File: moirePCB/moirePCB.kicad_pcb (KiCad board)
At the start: 2 copper layers, 37.1 x 85.7 mm, 25 parts, among them J1 USB_C_Receptacle, SW1 SW_Push_SPDT, SW3 SW_DPDT_x2, U1 ESP32-PICO-D4, U2 BQ24075RGT, U3 UA78M33, U4 RFM95W-915S2, U5 CH340E, Y2 32.768kHz

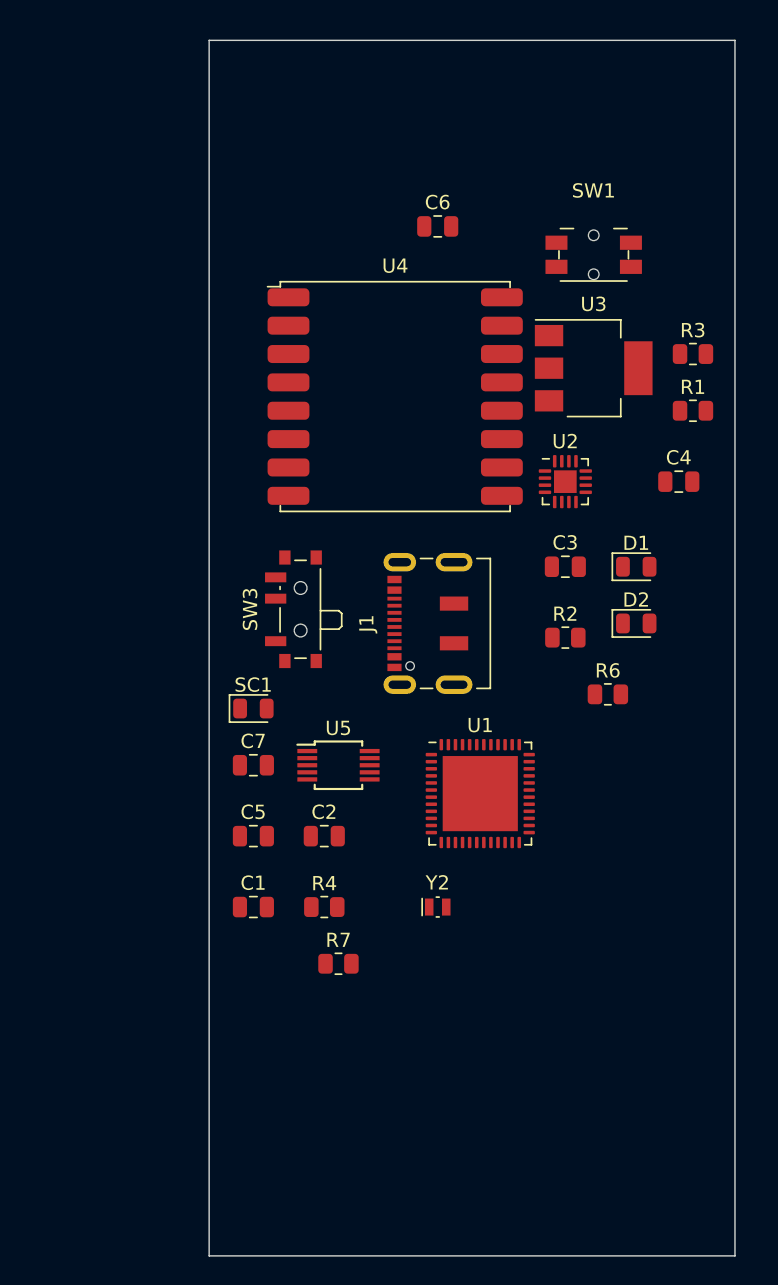
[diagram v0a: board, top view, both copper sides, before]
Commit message: new placement and battery footprint
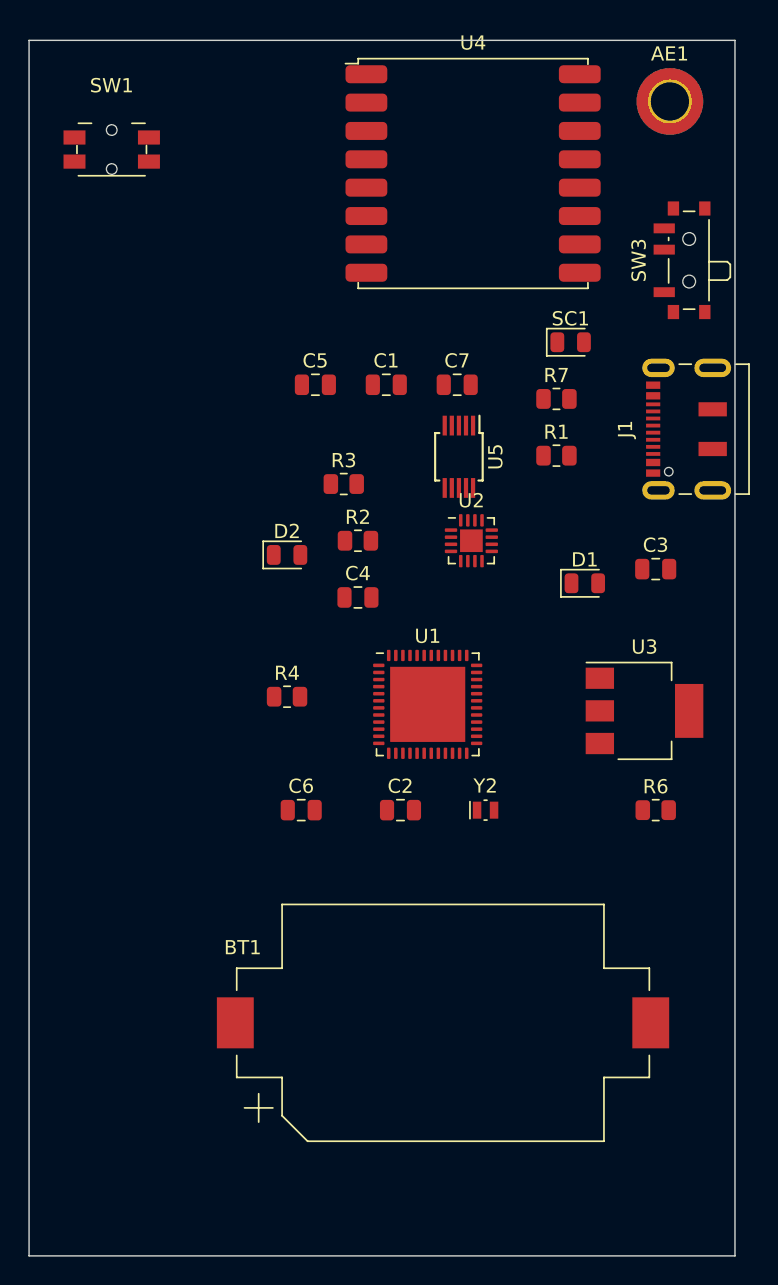
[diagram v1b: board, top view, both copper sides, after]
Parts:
- added AE1: T1-915M Antenna, MountingHole:MountingHole_2.7mm_M2.5_DIN965_Pad_TopBottom, F.Cu at (85.0, 33.0)
- added BT1: Battery_Cell, Battery:BatteryHolder_Keystone_1060_1x2032, F.Cu at (69.0, 98.0)
- moved R7 42.7 mm to (77.0, 54.0)
- moved C6 42.3 mm to (59.0, 83.0)
- moved C1 38.0 mm to (65.0, 53.0)
- moved SW3 36.8 mm to (86.0, 44.2)
- moved SW1 34.8 mm to (45.6, 36.4)
- moved SC1 34.2 mm to (78.0, 50.0)
- moved C5 32.1 mm to (60.0, 53.0)
- moved C7 30.4 mm to (70.0, 53.0)
- moved R3 26.3 mm to (62.0, 60.0)
- moved D2 25.1 mm to (58.0, 65.0)
- moved U3 24.4 mm to (83.2, 76.0)
- moved C4 24.1 mm to (63.0, 68.0)
- moved U5 23.4 mm to (70.1, 58.1), turned to -90 degrees
- moved J1 22.8 mm to (86.9, 56.1)
- moved U4 16.7 mm to (71.1, 38.1)
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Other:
- board size 37.1 x 85.7 mm -> 49.8 x 85.7 mm

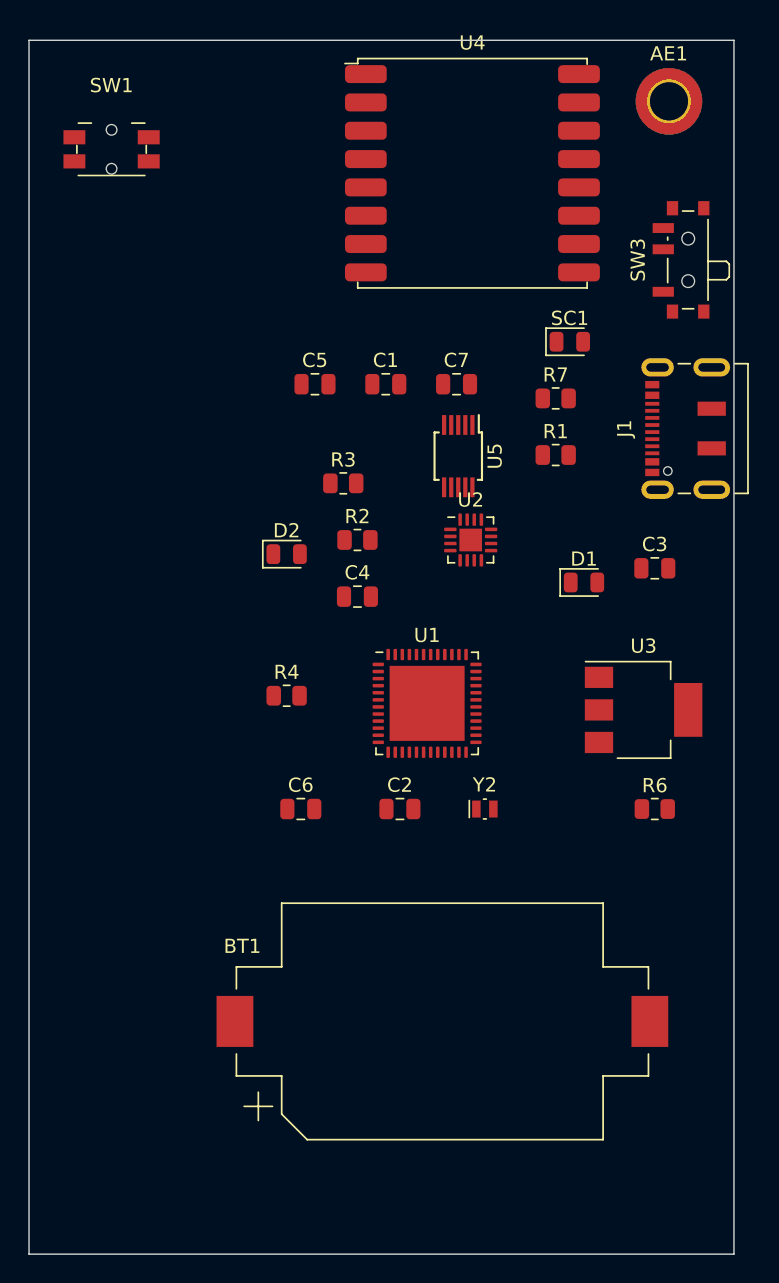
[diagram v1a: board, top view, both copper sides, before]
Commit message: ground plane, routing, comp layout
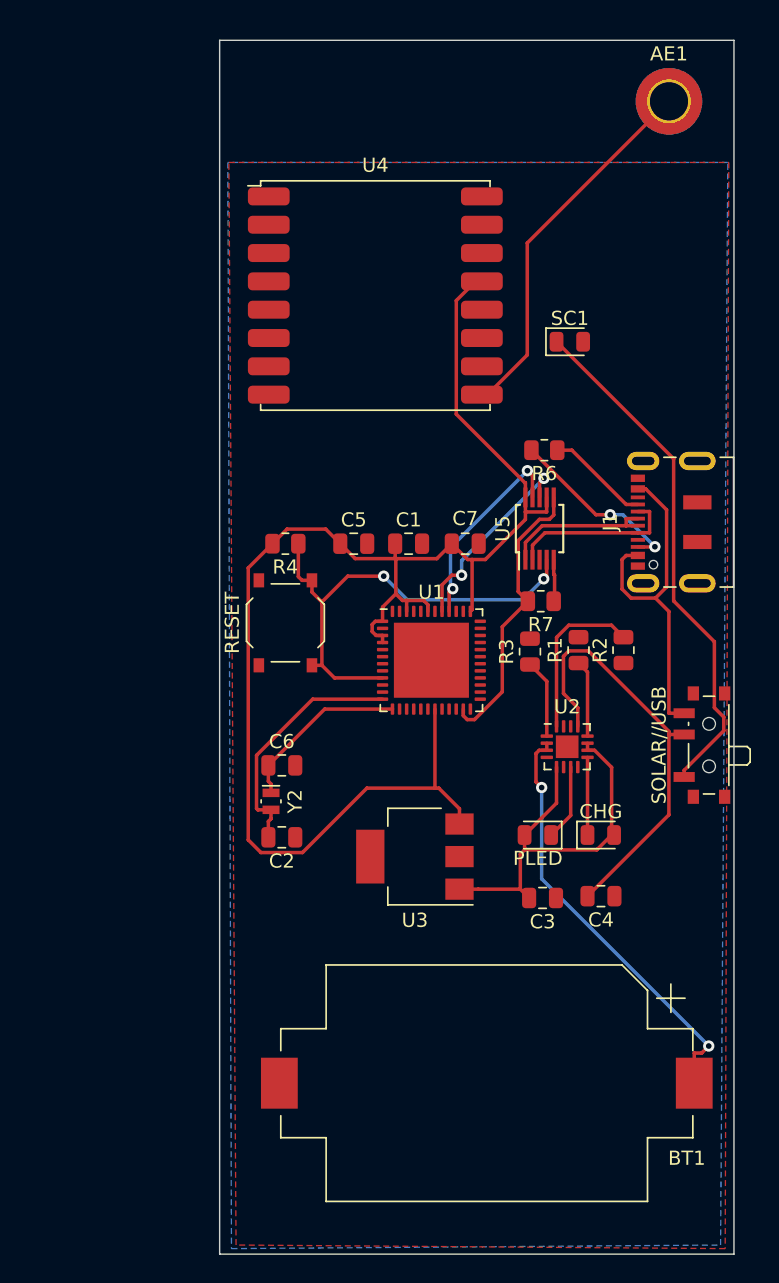
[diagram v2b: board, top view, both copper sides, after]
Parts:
- removed SW1: SW_Push_SPDT, Button_Switch_SMD:Panasonic_EVQPUL_EVQPUC
- added RESET: SW_Push, Button_Switch_SMD:SW_Push_1P1T_XKB_TS-1187A, F.Cu at (57.9, 69.8)
- moved SOLAR//USB 34.3 mm to (87.5, 78.5)
- moved CHG 29.8 mm to (80.2, 84.8)
- moved C4 27.3 mm to (80.2, 89.2), turned to 180 degrees
- moved R6 26.5 mm to (76.2, 57.7), turned to 180 degrees
- moved C3 24.6 mm to (76.1, 89.3), turned to 180 degrees
- moved R2 20.3 mm to (81.8, 71.8), turned to 90 degrees
- moved U3 19.2 mm to (67.1, 86.4), turned to 180 degrees
- moved PLED 18.1 mm to (75.7, 84.8), turned to 180 degrees
- moved R3 17.7 mm to (75.2, 71.9), turned to 90 degrees
- moved U2 16.1 mm to (77.8, 78.6)
- moved Y2 15.1 mm to (56.9, 82.5), turned to -90 degrees
- moved R7 14.4 mm to (75.9, 68.3), turned to 180 degrees
- moved R1 13.9 mm to (78.6, 71.8), turned to 90 degrees
- moved C5 11.6 mm to (62.7, 64.3)
- moved C1 11.4 mm to (66.6, 64.3)
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- renumbered D2 to CHG, D1 to PLED, SW3 to SOLAR//USB
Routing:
- net VCC: track 0.00 -> 105.7 mm
- net Net-(SC1-+): track 0.00 -> 36.8 mm
- net /EN: track 0.00 -> 34.2 mm, vias 0 -> 2
- net Net-(BT1-+): track 0.00 -> 30.4 mm, vias 0 -> 2
- net Net-(SW3A-B): track 0.00 -> 30.4 mm
- net Net-(D1-A): track 0.00 -> 29.1 mm
- net Net-(AE1-A): track 0.00 -> 26.4 mm
- net /USB5V: track 0.00 -> 24.7 mm
- net /IO0: track 0.00 -> 20.4 mm
- net Net-(U1-IO32): track 0.00 -> 17.4 mm
- net /RX: track 0.00 -> 14.4 mm, vias 0 -> 2
- net /TX: track 0.00 -> 14.3 mm, vias 0 -> 2
- net Net-(J1-CC1): track 0.00 -> 12.8 mm, vias 0 -> 2
- net Net-(U1-IO33): track 0.00 -> 12.4 mm
- net /D-: track 0.00 -> 12.0 mm
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- added copper zone on B.Cu, net GND
- added copper zone on F.Cu, net GND
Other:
- board size 49.8 x 85.7 mm -> 36.3 x 85.7 mm

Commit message: vias for esp32
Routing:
- net GND: track 0.00 -> 0.22 mm, vias 0 -> 9
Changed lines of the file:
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@@
   (segment (start 70.3566 66.4895) (end 70.3566 65.462) (width 0.25) (layer "B.Cu") (net 37))
   (segment (start 70.3566 65.462) (end 76.171 59.6476) (width 0.25) (layer "B.Cu") (net 37))
+  (segment (start 68.224 72.492) (end 68.216 72.5) (width 0.25) (layer "F.Cu") (net 43))
+  (segment (start 68.2 72.5) (end 68.2 72.516) (width 0.25) (layer "F.Cu") (net 43))
+  (segment (start 68.2 72.516) (end 68.326 72.39) (width 0.25) (layer "F.Cu") (net 43))
+  (segment (start 68.216 72.5) (end 68.2 72.5) (width 0.25) (layer "F.Cu") (net 43))
+  (via (at 69.6 71.2) (size 0.8) (drill 0.4) (layers "F.Cu" "B.Cu") (net 43))
+  (via (at 66.9 71.2) (size 0.8) (drill 0.4) (layers "F.Cu" "B.Cu") (net 43))
+  (via (at 66.9 72.5) (size 0.8) (drill 0.4) (layers "F.Cu" "B.Cu") (net 43))
+  (via (at 68.2 72.5) (size 0.8) (drill 0.4) (layers "F.Cu" "B.Cu") (net 43))
+  (via (at 68.2 71.2) (size 0.8) (drill 0.4) (layers "F.Cu" "B.Cu") (net 43))
+  (via (at 69.6 72.5) (size 0.8) (drill 0.4) (layers "F.Cu" "B.Cu") (net 43))
+  (via (at 69.6 73.8) (size 0.8) (drill 0.4) (layers "F.Cu" "B.Cu") (net 43))
+  (via (at 66.9 73.8) (size 0.8) (drill 0.4) (layers "F.Cu" "B.Cu") (net 43))
+  (via (at 68.2 73.8) (size 0.8) (drill 0.4) (layers "F.Cu" "B.Cu") (net 43))
   (segment (start 76.373 73.9835) (end 76.373 77.851) (width 0.25) (layer "F.Cu") (net 44))
   (segment (start 75.184 72.7945) (end 76.373 73.9835) (width 0.25) (layer "F.Cu") (net 44))

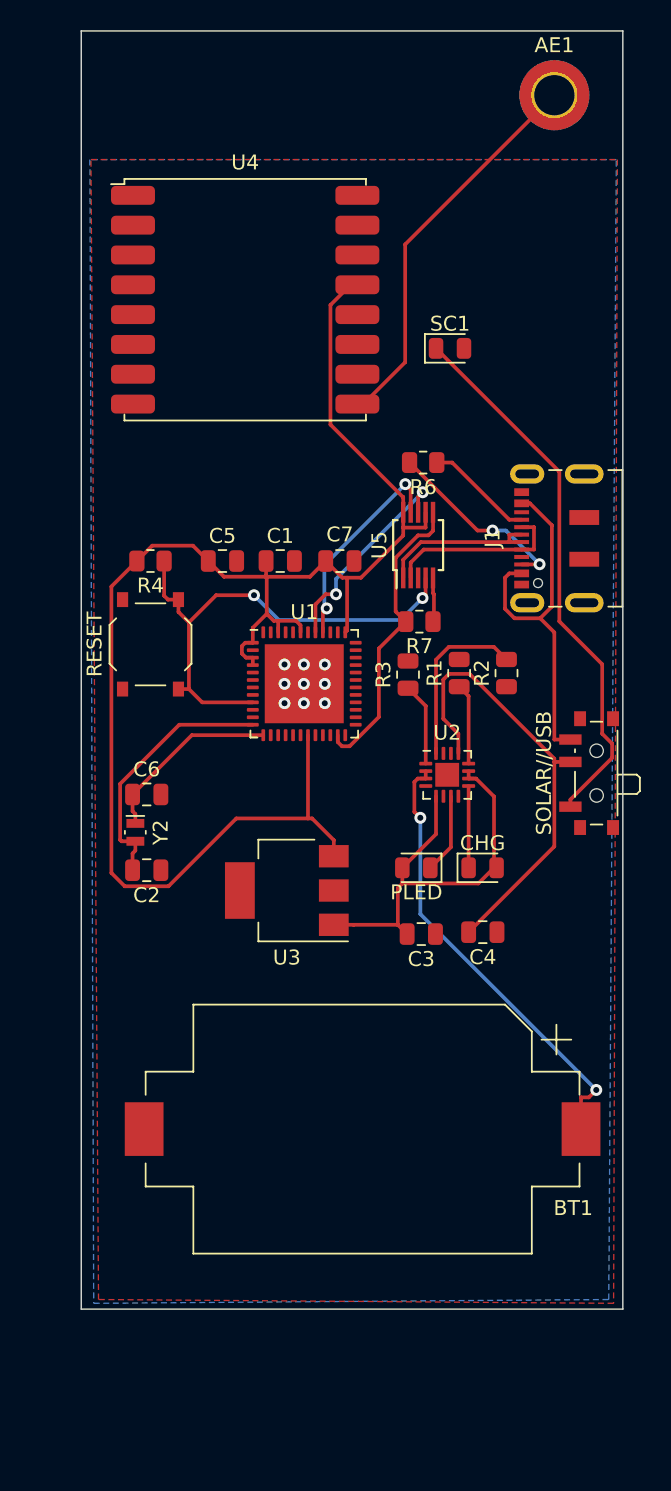
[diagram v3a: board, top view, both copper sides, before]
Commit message: pcb1 routing
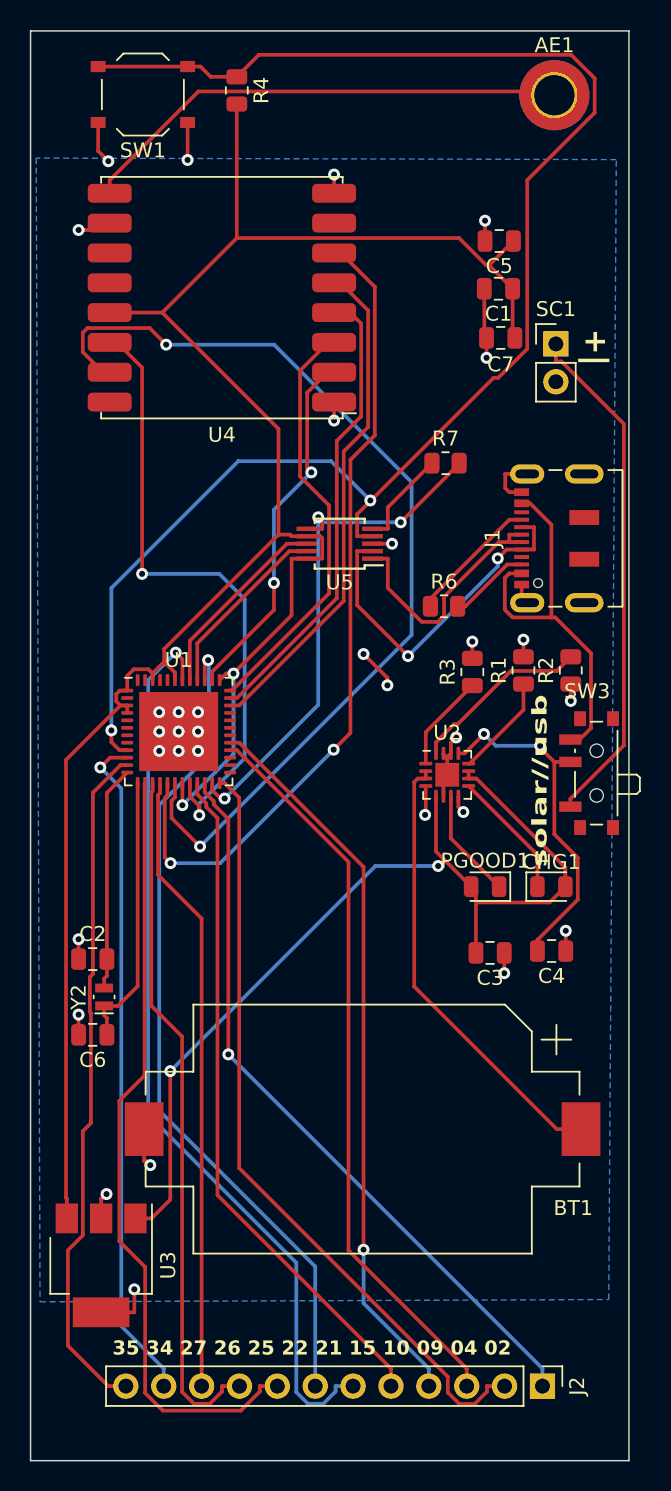
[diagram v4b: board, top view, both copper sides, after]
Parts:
- added J2: Conn_01x12_Pin, Connector_PinHeader_2.54mm:PinHeader_1x12_P2.54mm_Vertical, F.Cu at (84.2, 119.6)
- SC1: footprint LED_SMD:LED_0805_2012Metric -> Connector_PinHeader_2.54mm:PinHeader_1x02_P2.54mm_Vertical
- moved SW1 36.9 mm to (57.4, 33.0), turned to 180 degrees
- moved R4 32.1 mm to (63.7, 32.7), turned to -90 degrees
- moved C5 28.4 mm to (81.3, 42.8), turned to 180 degrees
- moved U3 28.1 mm to (54.6, 111.5), turned to -90 degrees
- moved C1 23.4 mm to (81.2, 46.0), turned to 180 degrees
- moved C7 18.4 mm to (81.4, 49.3), turned to 180 degrees
- moved C6 16.5 mm to (54.0, 96.0), turned to 180 degrees
- moved Y2 11.2 mm to (54.8, 93.5), turned to 90 degrees
- moved R7 10.8 mm to (77.7, 57.7), turned to 0 degrees
- moved R6 9.74 mm to (77.6, 67.3), turned to 0 degrees
- moved U1 9.01 mm to (59.8, 75.7)
- moved SC1 7.11 mm to (85.1, 49.7)
- moved C2 6.97 mm to (54.0, 91.0), turned to 0 degrees
- moved U5 5.26 mm to (70.6, 63.1), turned to 180 degrees
- moved C4 4.78 mm to (84.8, 90.4)
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- renumbered CHG to CHG1, PLED to PGOOD1, RESET to SW1, SOLAR//USB to SW3
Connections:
- U1 pad 10: unconnected-(U1-IO34-Pad10) -> /GPIO_34
- U1 pad 11: unconnected-(U1-IO35-Pad11) -> /GPIO_35
- U1 pad 14: unconnected-(U1-IO25-Pad14) -> /GPIO_25
- U1 pad 15: unconnected-(U1-IO26-Pad15) -> /GPIO_26
- U1 pad 16: unconnected-(U1-IO27-Pad16) -> /GPIO_27
- U1 pad 17: unconnected-(U1-IO14-Pad17) -> /GPIO_14
- U1 pad 18: unconnected-(U1-IO12-Pad18) -> /GPIO_12
- U1 pad 20: unconnected-(U1-IO13-Pad20) -> /GPIO_13
- U1 pad 21: unconnected-(U1-IO15-Pad21) -> /GPIO_15
- U1 pad 22: unconnected-(U1-IO2-Pad22) -> /GPIO_2
- U1 pad 24: unconnected-(U1-IO4-Pad24) -> /GPIO_4
- U1 pad 28: unconnected-(U1-SD2/IO9-Pad28) -> /GPIO_9
- U1 pad 29: unconnected-(U1-SD3/IO10-Pad29) -> /GPIO_10
- U1 pad 34: unconnected-(U1-IO5-Pad34) -> /GPIO_5
- U1 pad 35: unconnected-(U1-IO18-Pad35) -> /GPIO_18
- U1 pad 36: unconnected-(U1-IO23-Pad36) -> /GPIO_23
- U1 pad 38: unconnected-(U1-IO19-Pad38) -> /GPIO_19
- U1 pad 39: unconnected-(U1-IO22-Pad39) -> /GPIO_22
- U1 pad 42: unconnected-(U1-IO21-Pad42) -> /GPIO_21
- U4 pad 14: unconnected-(U4-DIO0-Pad14) -> /GPIO_13
- U4 pad 15: unconnected-(U4-DIO1-Pad15) -> /GPIO_12
- U4 pad 2: unconnected-(U4-MISO-Pad2) -> /GPIO_19
- U4 pad 3: unconnected-(U4-MOSI-Pad3) -> /GPIO_23
- U4 pad 4: unconnected-(U4-SCK-Pad4) -> /GPIO_18
- U4 pad 5: unconnected-(U4-NSS-Pad5) -> /GPIO_5
- U4 pad 6: unconnected-(U4-RESET-Pad6) -> /GPIO_14
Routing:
- net /EN: track 34.2 -> 107.0 mm
- net /GPIO_12: track 0.00 -> 65.6 mm, vias 0 -> 2
- net /GPIO_21: track 0.00 -> 61.3 mm, vias 0 -> 1
- net /GPIO_22: track 0.00 -> 55.9 mm, vias 0 -> 1
- net /GPIO_14: track 0.00 -> 55.6 mm, vias 0 -> 2
- net /GPIO_25: track 0.00 -> 52.6 mm
- net /GPIO_4: track 0.00 -> 52.2 mm
- net GND: track 0.22 -> 50.2 mm, vias 9 -> 32
- net /GPIO_2: track 0.00 -> 49.8 mm, vias 0 -> 1
- net /GPIO_9: track 0.00 -> 49.5 mm
- net /GPIO_10: track 0.00 -> 49.0 mm, vias 0 -> 1
- net /GPIO_26: track 0.00 -> 46.6 mm
- net /GPIO_35: track 0.00 -> 45.9 mm
- net /GPIO_15: track 0.00 -> 45.8 mm
- net /GPIO_34: track 0.00 -> 45.3 mm, vias 0 -> 1
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- removed copper zone on F.Cu, net GND
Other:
- board size 36.3 x 85.7 mm -> 40.1 x 95.9 mm
- board text added: "+|"
- board text added: "35 34 27 26 25 22 21 15 10 09 04 02"
- board text added: "solar//usb"

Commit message: New Pins
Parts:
- added CLK1: Conn_01x02_Pin, Connector_PinSocket_2.54mm:PinSocket_1x02_P2.54mm_Vertical, F.Cu at (78.2, 120.9)
- added GND1: Conn_01x03_Pin, Connector_PinSocket_2.54mm:PinSocket_1x03_P2.54mm_Vertical, F.Cu at (53.9, 120.9)
- added ONOFF1: SW_DPDT_x2, Button_Switch_SMD:SW_SPDT_PCM12, F.Cu at (87.3, 42.2)
- added VCC1: Conn_01x03_Pin, Connector_PinSocket_2.54mm:PinSocket_1x03_P2.54mm_Vertical, F.Cu at (65.7, 120.9)
- J2: footprint Connector_PinHeader_2.54mm:PinHeader_1x12_P2.54mm_Vertical -> Connector_PinSocket_2.54mm:PinSocket_1x12_P2.54mm_Vertical
- moved J2 8.34 mm to (80.9, 127.3)
- moved U5 0.27 mm to (70.6, 63.4)
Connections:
- U2 pad 15: GND -> Net-(ONOFF1A-B)
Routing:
- net VCC: track 148.3 -> 221.9 mm
- net /GPIO_18: track 31.1 -> 87.9 mm, vias 0 -> 2
- net Net-(ONOFF1A-B): track 0.00 -> 40.8 mm, vias 0 -> 2
- net GND: track 50.2 -> 80.4 mm, vias 32 -> 29
- net /GPIO_12: track 65.6 -> 41.6 mm
- net /EN: track 107.0 -> 86.0 mm
- net /GPIO_22: track 55.9 -> 74.4 mm
- net /GPIO_34: track 45.3 -> 57.8 mm, vias 1 -> 0
- net /GPIO_2: track 49.8 -> 61.0 mm
- net /GPIO_27: track 41.7 -> 52.3 mm, vias 0 -> 1
- net /GPIO_21: track 61.3 -> 71.3 mm
- net /GPIO_4: track 52.2 -> 59.9 mm
- net /GPIO_14: track 55.6 -> 63.0 mm
- net Net-(SW3A-B): track 23.4 -> 30.6 mm, vias 2 -> 0
- net /GPIO_9: track 49.5 -> 56.5 mm, vias 0 -> 1
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- added copper zone on F.Cu, net GND
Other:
- board size 40.1 x 95.9 mm -> 40.1 x 101.6 mm

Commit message: sensor
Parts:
- added C8: 10n, Capacitor_SMD:C_0805_2012Metric, F.Cu at (145.9, 56.4)
- added C9: 100n, Capacitor_SMD:C_0805_2012Metric, F.Cu at (145.9, 59.4)
- added R5: 10k, Resistor_SMD:R_0805_2012Metric, F.Cu at (150.3, 56.4)
- added R8: 1M, Resistor_SMD:R_0805_2012Metric, F.Cu at (150.3, 59.3)
- added U6: TLC555xD, Package_SO:SOIC-8_3.9x4.9mm_P1.27mm, F.Cu at (147.9, 51.7)
- moved J2 43.2 mm to (44.2, 104.4), turned to 0 degrees
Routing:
- net GND: track 80.4 -> 203.2 mm, vias 29 -> 0
- net VCC: track 221.9 -> 108.6 mm, vias 2 -> 0
- net /GPIO_18: track 87.9 -> 0.00 mm, vias 2 -> 0
- net /EN: track 86.0 -> 0.00 mm, vias 2 -> 0
- net /GPIO_22: track 74.4 -> 0.00 mm, vias 1 -> 0
- net /GPIO_21: track 71.3 -> 0.00 mm, vias 1 -> 0
- net Net-(CHG1-A): track 65.4 -> 0.00 mm, vias 2 -> 0
- net /GPIO_14: track 63.0 -> 0.00 mm, vias 2 -> 0
- net /GPIO_2: track 61.0 -> 0.00 mm, vias 1 -> 0
- net /GPIO_4: track 59.9 -> 0.00 mm
- net /GPIO_34: track 57.8 -> 0.00 mm
- net /GPIO_9: track 56.5 -> 0.00 mm, vias 1 -> 0
- net /GPIO_10: track 55.5 -> 0.00 mm
- net /GPIO_25: track 55.0 -> 0.00 mm
- net /GPIO_35: track 52.5 -> 0.00 mm
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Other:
- board outline removed
